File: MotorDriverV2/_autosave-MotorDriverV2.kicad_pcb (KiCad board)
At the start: 2 copper layers, 12 parts, among them IC1 DRV8871DDARQ1, IC2 DRV8871DDARQ1, IC3 ESP32-S2FH4, J1 Power, J2 Out_A, J3 Out_A, J4 Out_B, J5 Out_B

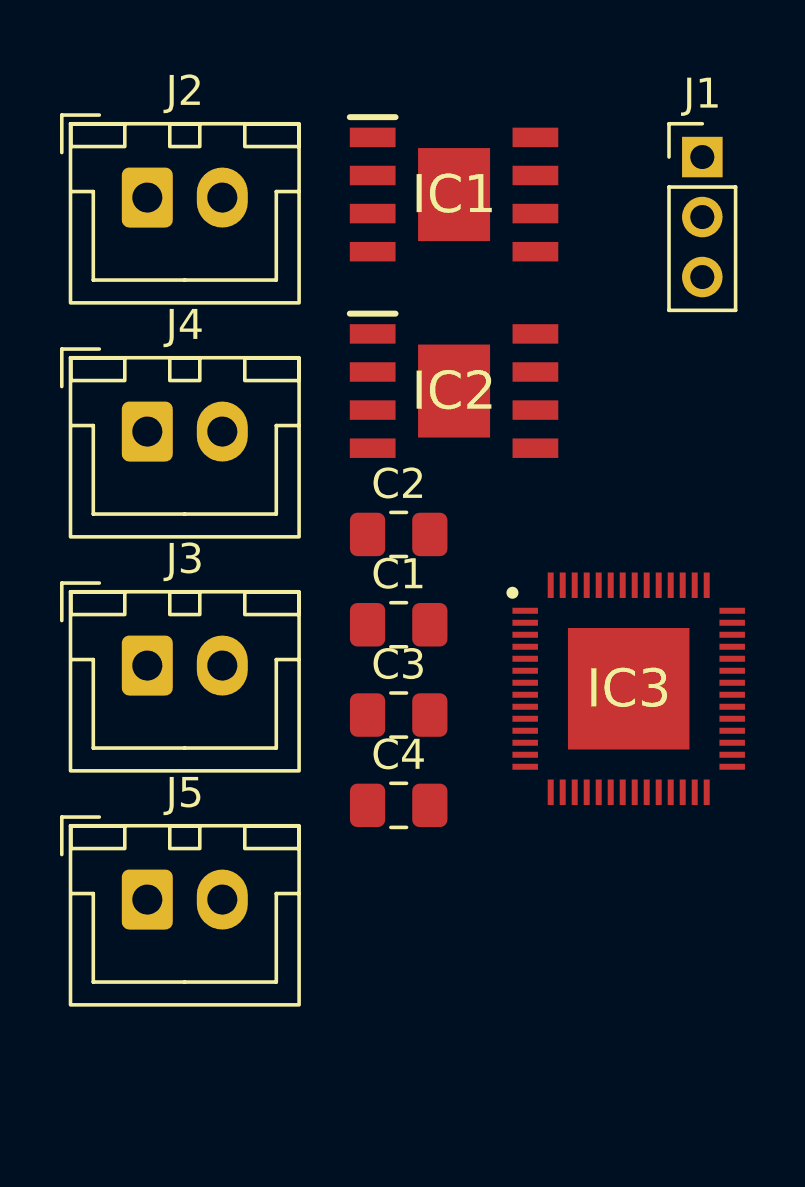
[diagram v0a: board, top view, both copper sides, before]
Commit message: UPDATE: Added symbols, fotprints and datasheets for components
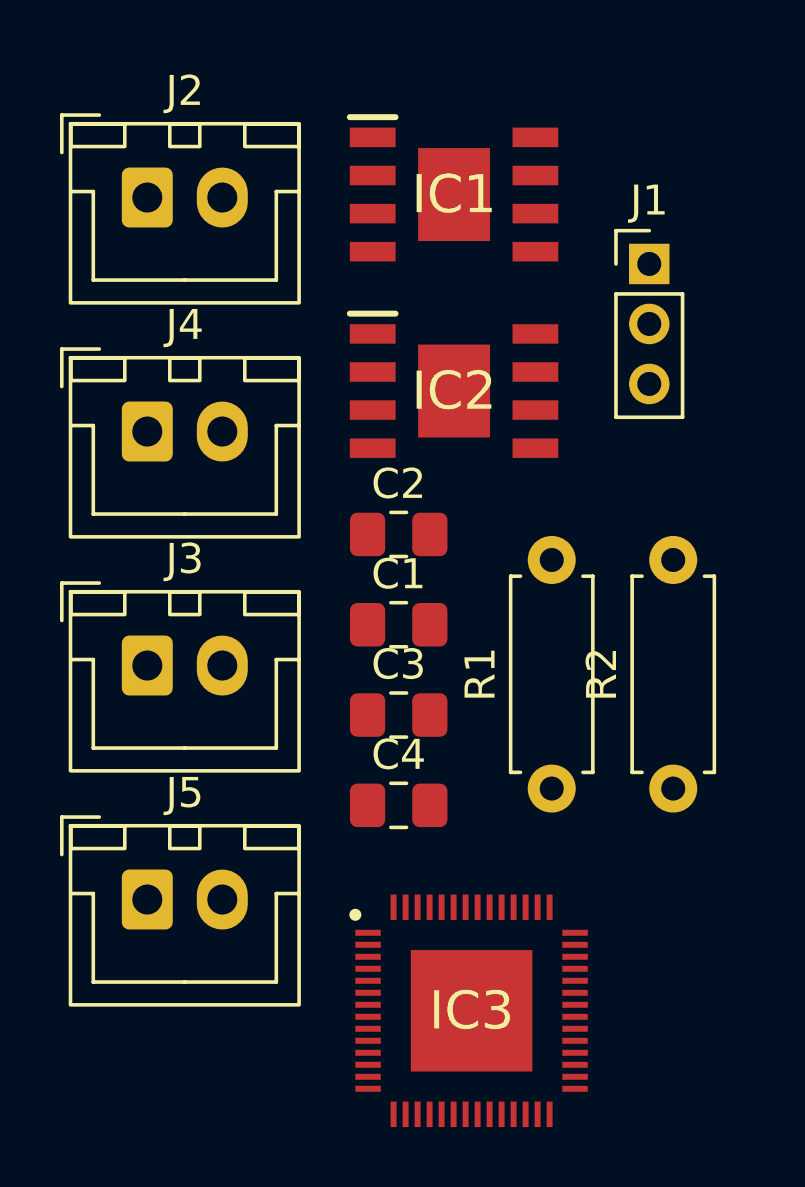
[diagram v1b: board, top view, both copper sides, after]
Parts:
- added R1: 14.8K, Resistor_THT:R_Axial_DIN0207_L6.3mm_D2.5mm_P7.62mm_Horizontal, F.Cu at (137.8, 90.1)
- added R2: 14.8K, Resistor_THT:R_Axial_DIN0207_L6.3mm_D2.5mm_P7.62mm_Horizontal, F.Cu at (141.8, 90.1)
- moved IC3 11.9 mm to (135.1, 97.5)
- moved J1 3.98 mm to (141.0, 72.6)
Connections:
- J2 pad 1: In1_2 -> In1_1
- J2 pad 2: In1_1 -> In1_2
